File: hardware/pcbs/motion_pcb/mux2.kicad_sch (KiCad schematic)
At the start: 5 parts, among them Q1 BSS138, U42 SN74LVC1T45DBV

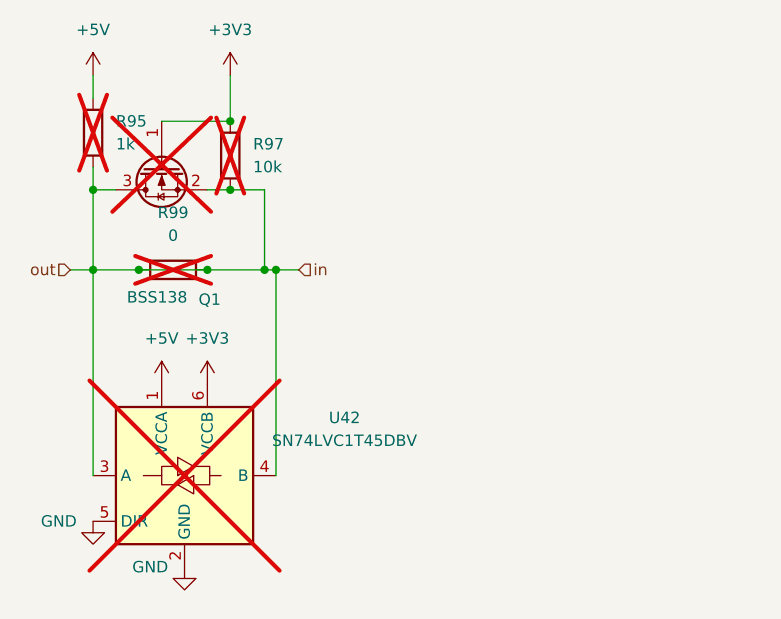
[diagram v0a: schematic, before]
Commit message: changing labels
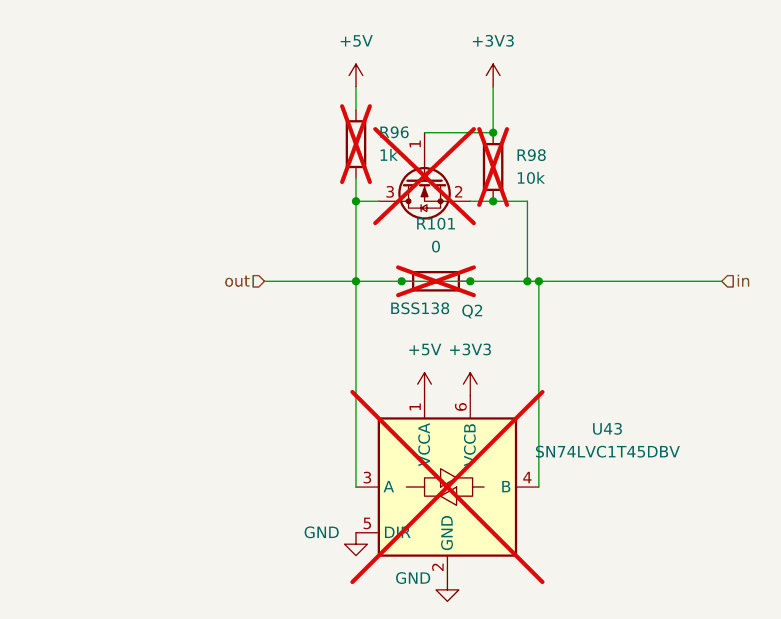
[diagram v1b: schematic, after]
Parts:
- removed Q1: BSS138, Package_TO_SOT_SMD:SOT-23, symbol Transistor_FET:BSS138
- removed R95: 1k, Resistor_SMD:R_1206_3216Metric_Pad1.30x1.75mm_HandSolder, symbol Device:R
- removed R97: 10k, Resistor_SMD:R_1206_3216Metric_Pad1.30x1.75mm_HandSolder, symbol Device:R
- removed R99: 0, Resistor_SMD:R_1206_3216Metric_Pad1.30x1.75mm_HandSolder, symbol Device:R
- removed U42: SN74LVC1T45DBV, Package_TO_SOT_SMD:SOT-23-6, symbol Logic_LevelTranslator:SN74LVC1T45DBV
- added Q2: BSS138, Package_TO_SOT_SMD:SOT-23, symbol Transistor_FET:BSS138
- added R101: 0, Resistor_SMD:R_1206_3216Metric_Pad1.30x1.75mm_HandSolder, symbol Device:R
- added R96: 1k, Resistor_SMD:R_1206_3216Metric_Pad1.30x1.75mm_HandSolder, symbol Device:R
- added R98: 10k, Resistor_SMD:R_1206_3216Metric_Pad1.30x1.75mm_HandSolder, symbol Device:R
- added U43: SN74LVC1T45DBV, Package_TO_SOT_SMD:SOT-23-6, symbol Logic_LevelTranslator:SN74LVC1T45DBV
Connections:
- net +3V3: now also Q2.1 (G), R98.1, U43.6 (VCCB)
- net +5V: now also R96.1, U43.1 (VCCA)
- net GND: now also U43.2 (GND), U43.5 (DIR)
- net in: now also Q2.2 (S), Q2.3 (D), R101.1, R101.2, R96.2, R98.2, U43.3 (A), U43.4 (B)
